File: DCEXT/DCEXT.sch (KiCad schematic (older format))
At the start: 22 parts, among them J3 USB1015-XX-X-X_REVC, J4 USB1015-XX-X-X_REVC, J5 FAN_CON, J6 Conn_02x25_Odd_Even, Q1 BSS138, U1 MPCIE-DevTerm, U2 USBUF02W6, U3 USBUF02W6, U4 SY6280

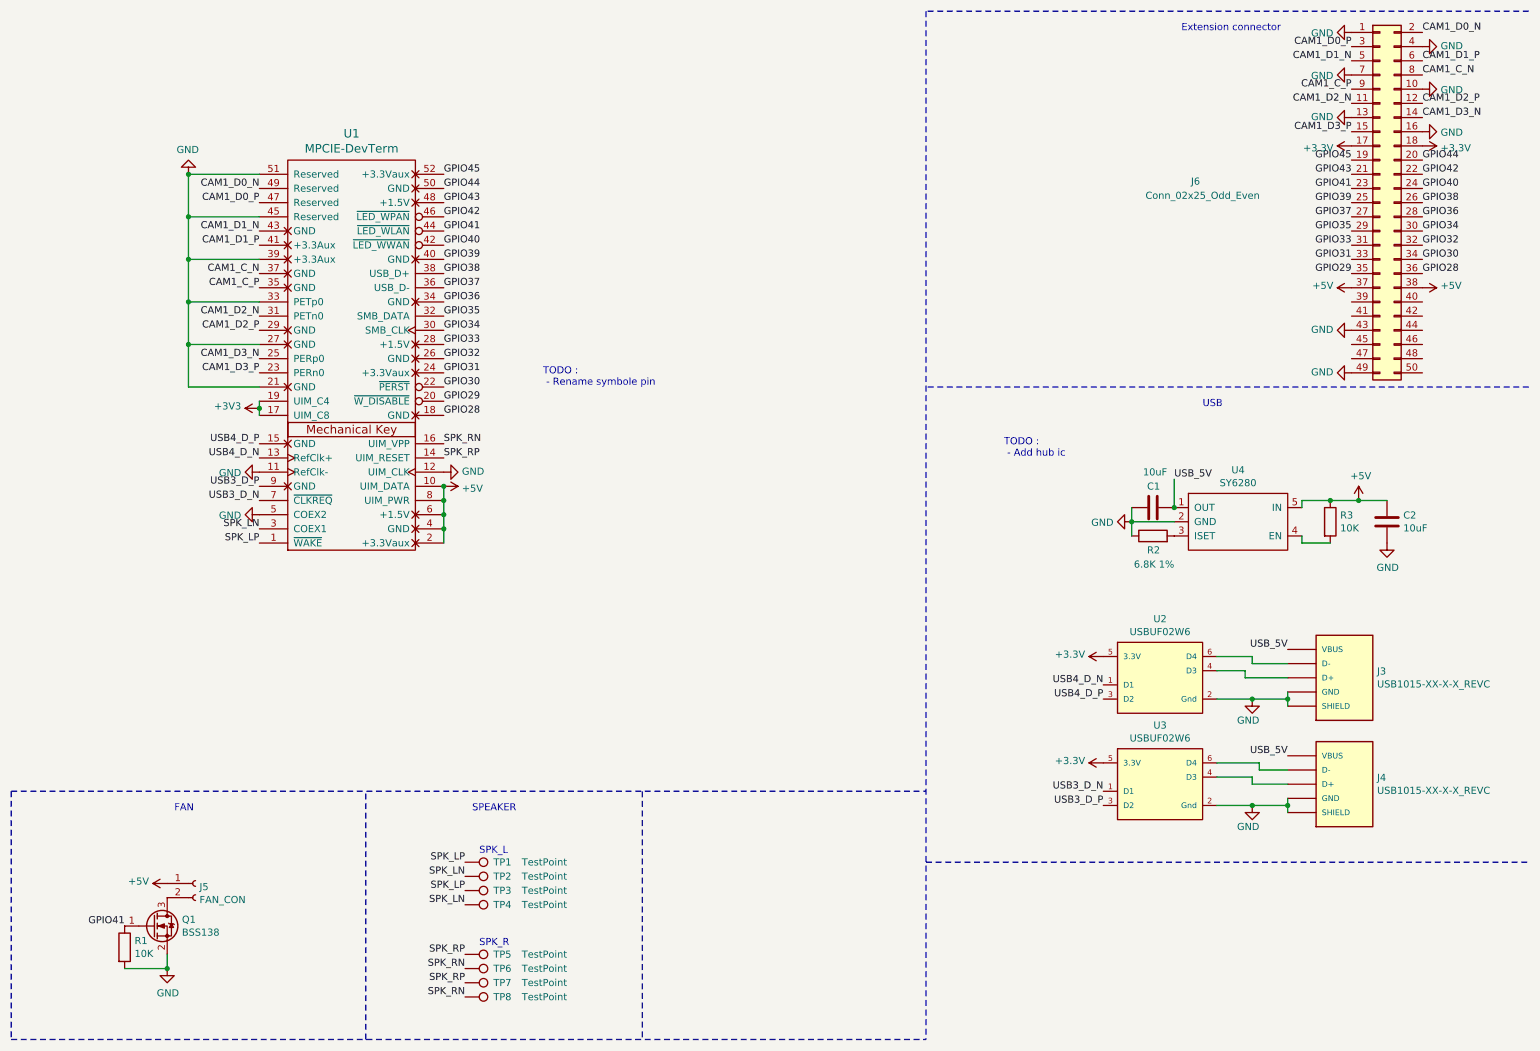
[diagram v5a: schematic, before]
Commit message: Add USB hub, routing and start part sourcing
Spoiller alert : everything is out of stock ...
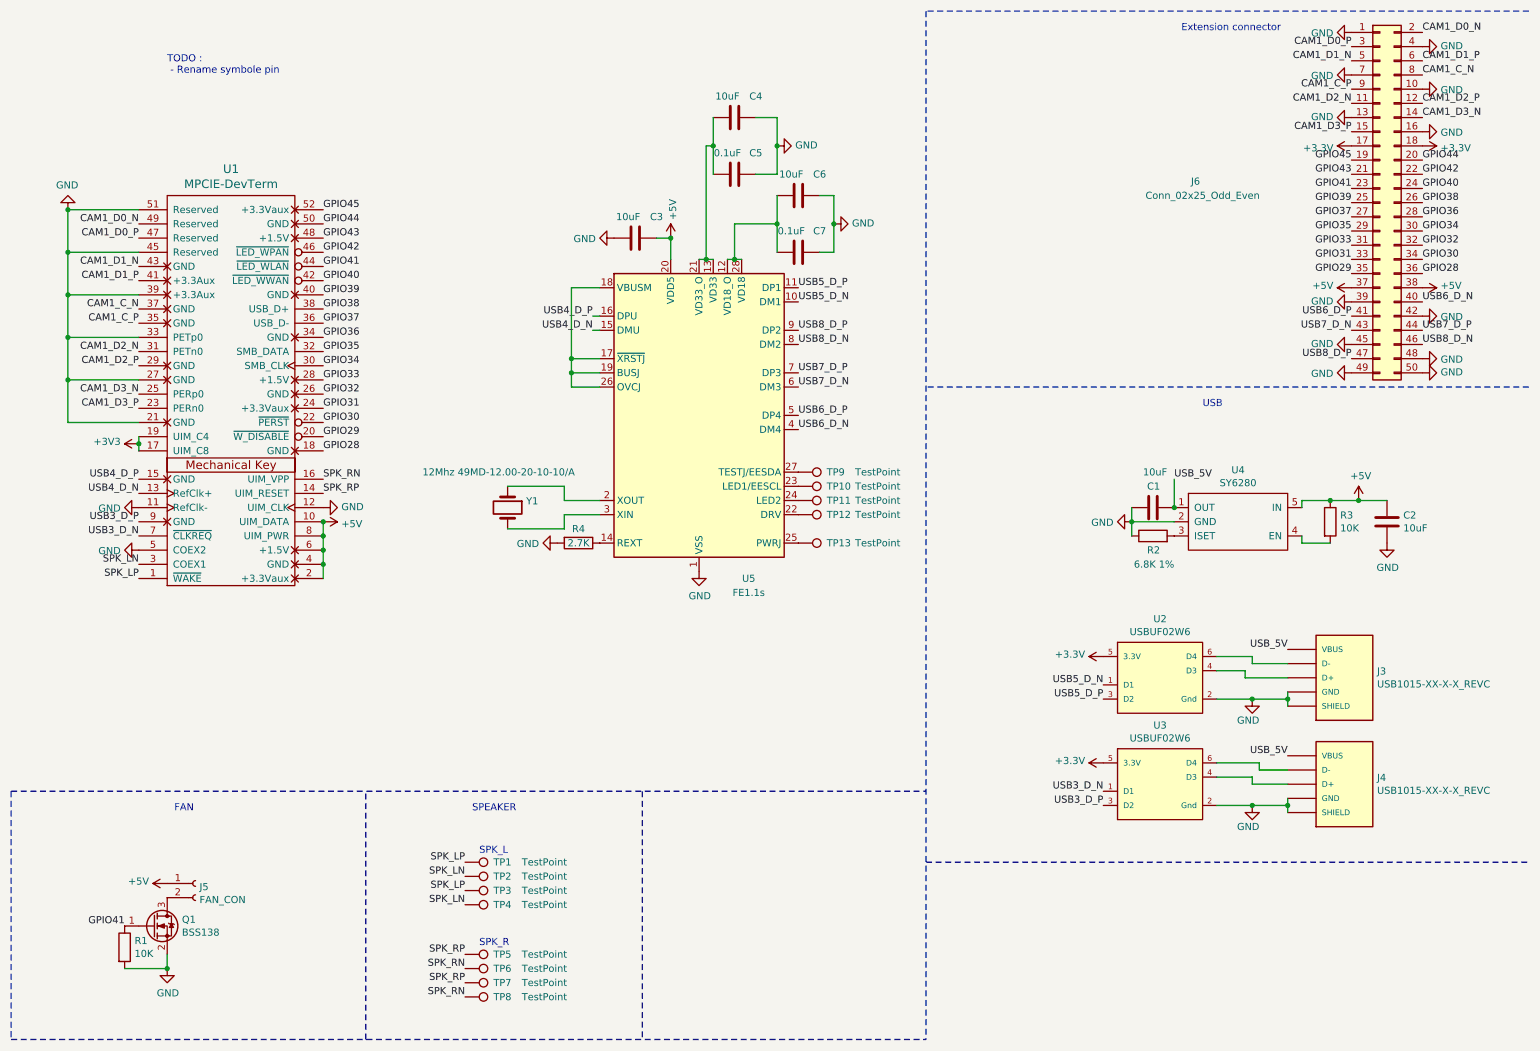
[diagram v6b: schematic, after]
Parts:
- added C3, C4, C6: 10uF, Capacitor_SMD:C_0402_1005Metric, symbol Device:C
- added C5, C7: 0.1uF, Capacitor_SMD:C_0402_1005Metric, symbol Device:C
- added R4: 2.7K, Resistor_SMD:R_0402_1005Metric, symbol Device:R
- added TP10, TP11, TP12, TP13, TP9: TestPoint, TestPoint:TestPoint_Pad_1.5x1.5mm, symbol Connector:TestPoint
- added U5: FE1.1s, Package_SO:SSOP-28_3.9x9.9mm_P0.635mm, symbol Interface_USB:FE1.1s
- added Y1: 12Mhz 49MD-12.00-20-10-10/A, Crystal:Crystal_SMD_HC49-SD, symbol Device:Crystal
- C1, C2: footprint Capacitor_SMD:C_0402_1005Metric_Pad0.74x0.62mm_HandSolder -> Capacitor_SMD:C_0402_1005Metric
- J5: LCSC (none) -> C160237
- J6: LCSC (none) -> C11098
- Q1: LCSC (none) -> C427380
- R1, R2, R3: footprint Resistor_SMD:R_0402_1005Metric_Pad0.72x0.64mm_HandSolder -> Resistor_SMD:R_0402_1005Metric
- U2, U3: LCSC (none) -> C74936
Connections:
- net +5V: now also C3.1, U5.20 (VDD5)
- net GND: now also J6.39 (Pin_39), J6.42 (Pin_42), J6.45 (Pin_45), J6.48 (Pin_48), J6.50 (Pin_50), C3.2, C4.1, C5.1, C6.1, C7.1, R4.2, U5.1 (VSS); no longer J6.43 (Pin_43)
- net USB4_D_N: now also U5.15 (DMU); no longer U2.1 (D1)
- net USB4_D_P: now also U5.16 (DPU); no longer U2.3 (D2)
- net USB6_D_N: now reaches J6.40 (Pin_40)
- net USB6_D_N: now also U5.4 (DM4)
- net USB6_D_P: now reaches J6.41 (Pin_41)
- net USB6_D_P: now also U5.5 (DP4)
- net USB7_D_P: now reaches J6.44 (Pin_44)
- net USB7_D_P: now also U5.7 (DP3)
- net USB8_D_N: now reaches J6.46 (Pin_46)
- net USB8_D_N: now also U5.8 (DM2)
- net USB8_D_P: now reaches J6.47 (Pin_47)
- net USB8_D_P: now also U5.9 (DP2)
- new net: C6.2, C7.2, U5.12 (VD18_O), U5.28 (VD18)
- new net: C4.2, C5.2, U5.13 (VD33), U5.21 (VD33_O)
- new net: R4.1, U5.14 (REXT)
- new net: U5.17 (~XRSTJ), U5.18 (VBUSM), U5.19 (BUSJ), U5.26 (OVCJ)
- new net: U5.2 (XOUT), Y1.1
- new net: TP12.1, U5.22 (DRV)
- new net: TP10.1, U5.23 (LED1/EESCL)
- new net: TP11.1, U5.24 (LED2)
- new net: TP13.1, U5.25 (PWRJ)
- new net: TP9.1, U5.27 (TESTJ/EESDA)
- new net: U5.3 (XIN), Y1.2
- new net USB5_D_N: U2.1 (D1), U5.10 (DM1)
- new net USB5_D_P: U2.3 (D2), U5.11 (DP1)
- new net USB7_D_N: J6.43 (Pin_43), U5.6 (DM3)
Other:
- note removed: "TODO :\n - Add hub ic"
- moved on the sheet: U1

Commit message: Change USB connector to something in stock :/ + gerber files
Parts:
- C1, C2, C3, C4, C6: LCSC (none) -> C2846677
- C5, C7: LCSC (none) -> C41851
- J3, J4: value USB1015-XX-X-X_REVC -> 905-351A2032D10100; footprint DCEXT:GCT_USB1015-XX-X-X_REVC -> DCEXT:USB-A-TH_USB-M-55-F; LCSC (none) -> C42623
- R1, R3: LCSC (none) -> C258091
- R2: LCSC (none) -> C208929
- R4: LCSC (none) -> C168220
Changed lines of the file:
@@
 P 9900 5200
 F 0 "J3" H 10130 5246 50  0000 L CNN
-F 1 "USB1015-XX-X-X_REVC" H 10130 5155 50  0000 L CNN
-F 2 "DCEXT:GCT_USB1015-XX-X-X_REVC" H 9900 5200 50  0001 L BNN
+F 1 "905-351A2032D10100" H 10130 5155 50  0000 L CNN
+F 2 "DCEXT:USB-A-TH_USB-M-55-F" H 9900 5200 50  0001 L BNN
 F 3 "" H 9900 5200 50  0001 L BNN
 F 4 "GCT" H 9900 5200 50  0001 L BNN "MANUFACTURER"
+F 5 "C42623" H 9900 5200 50  0001 C CNN "LCSC"
 	1    9900 5200
 	1    0    0    -1
@@
 P 9900 5950
 F 0 "J4" H 10130 5996 50  0000 L CNN
-F 1 "USB1015-XX-X-X_REVC" H 10130 5905 50  0000 L CNN
-F 2 "DCEXT:GCT_USB1015-XX-X-X_REVC" H 9900 5950 50  0001 L BNN
+F 1 "905-351A2032D10100" H 10130 5905 50  0000 L CNN
+F 2 "DCEXT:USB-A-TH_USB-M-55-F" H 9900 5950 50  0001 L BNN
 F 3 "" H 9900 5950 50  0001 L BNN
 F 4 "GCT" H 9900 5950 50  0001 L BNN "MANUFACTURER"
+F 5 "C42623" H 9900 5950 50  0001 C CNN "LCSC"
 	1    9900 5950
 	1    0    0    -1
@@
 F 2 "Resistor_SMD:R_0402_1005Metric" V 1230 7100 50  0001 C CNN
 F 3 "~" H 1300 7100 50  0001 C CNN
+F 4 "C258091" H 1300 7100 50  0001 C CNN "LCSC"
 	1    1300 7100
 	1    0    0    -1
@@
 F 2 "Resistor_SMD:R_0402_1005Metric" V 8480 4200 50  0001 C CNN
 F 3 "~" H 8550 4200 50  0001 C CNN
+F 4 "C208929" V 8550 4200 50  0001 C CNN "LCSC"
 	1    8550 4200
 	0    -1   -1   0
@@
 F 2 "Capacitor_SMD:C_0402_1005Metric" H 8588 3850 50  0001 C CNN
 F 3 "~" H 8550 4000 50  0001 C CNN
+F 4 "C2846677" V 8550 4000 50  0001 C CNN "LCSC"
 	1    8550 4000
 	0    -1   -1   0
@@
 F 2 "Resistor_SMD:R_0402_1005Metric" V 9730 4100 50  0001 C CNN
 F 3 "~" H 9800 4100 50  0001 C CNN
+F 4 "C258091" H 9800 4100 50  0001 C CNN "LCSC"
 	1    9800 4100
 	1    0    0    -1
@@
 F 2 "Capacitor_SMD:C_0402_1005Metric" H 10238 3950 50  0001 C CNN
 F 3 "~" H 10200 4100 50  0001 C CNN
+F 4 "C2846677" H 10200 4100 50  0001 C CNN "LCSC"
 	1    10200 4100
 	1    0    0    -1
@@
 F 2 "Resistor_SMD:R_0402_1005Metric" V 4430 4250 50  0001 C CNN
 F 3 "~" H 4500 4250 50  0001 C CNN
+F 4 "C168220" V 4500 4250 50  0001 C CNN "LCSC"
 	1    4500 4250
 	0    1    1    0
@@
 F 2 "Capacitor_SMD:C_0402_1005Metric" H 6088 2050 50  0001 C CNN
 F 3 "~" H 6050 2200 50  0001 C CNN
+F 4 "C41851" V 6050 2200 50  0001 C CNN "LCSC"
 	1    6050 2200
 	0    1    1    0
@@
 F 2 "Capacitor_SMD:C_0402_1005Metric" H 5638 1500 50  0001 C CNN
 F 3 "~" H 5600 1650 50  0001 C CNN
+F 4 "C41851" V 5600 1650 50  0001 C CNN "LCSC"
 	1    5600 1650
 	0    1    1    0
@@
 F 2 "Capacitor_SMD:C_0402_1005Metric" H 6088 1650 50  0001 C CNN
 F 3 "~" H 6050 1800 50  0001 C CNN
+F 4 "C2846677" V 6050 1800 50  0001 C CNN "LCSC"
 	1    6050 1800
 	0    1    1    0
@@
 F 2 "Capacitor_SMD:C_0402_1005Metric" H 5638 1100 50  0001 C CNN
 F 3 "~" H 5600 1250 50  0001 C CNN
+F 4 "C2846677" V 5600 1250 50  0001 C CNN "LCSC"
 	1    5600 1250
 	0    1    1    0
@@
 F 2 "Capacitor_SMD:C_0402_1005Metric" H 4938 1950 50  0001 C CNN
 F 3 "~" H 4900 2100 50  0001 C CNN
+F 4 "C2846677" V 4900 2100 50  0001 C CNN "LCSC"
 	1    4900 2100
 	0    1    1    0
